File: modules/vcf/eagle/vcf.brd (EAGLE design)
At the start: 100 x 87.6 mm, 78 parts, among them IC1 TL074P, IC2 LM13700N, IC3 TL074P, Q1 2N3906, Q2 2N3906, X1 22-23-2031, X10 AUDIO INPUTS, X11 POWER, X12 FILTER OUT, X2 CV INPUTS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

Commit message: Badly finish VCF board layout (single)
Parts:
- moved R38 174.2 mm to (84.5, 12.7), turned to 90 degrees
- moved R37 148.5 mm to (65.4, 9.53), turned to 90 degrees
- moved LED5 141.4 mm to (61.6, 23.5), turned to 180 degrees
- moved R32 139.2 mm to (74.9, 33.7), turned to 180 degrees
- moved C5 134.5 mm to (77.5, 29.2), turned to 180 degrees
- moved C16 129.6 mm to (81.9, 10.2), turned to 270 degrees
- moved LED4 128.9 mm to (61.6, 38.1), turned to 180 degrees
- moved R39 126.8 mm to (93.3, 40.6), turned to 270 degrees
- moved R27 120.3 mm to (66.0, 36.2), turned to 90 degrees
- moved R20 119.7 mm to (84.5, 24.8), turned to 270 degrees
- moved R34 119.6 mm to (81.3, 62.9), turned to 90 degrees
- moved LED3 117.6 mm to (61.6, 45.1)
- moved R36 117.2 mm to (74.9, 5.71), turned to 180 degrees
- moved C11 116.5 mm to (81.9, 22.9), turned to 90 degrees
- moved R30 115.1 mm to (68.6, 30.5), turned to 90 degrees
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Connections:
- net N$1 renamed N$1V-OCT
- net N$31 renamed N$LP-OUT
- net N$40 renamed N$BP-OUT
- net N$51 renamed N$HP-OUT
- removed net N$6: X10.2, X7.2
- new net N$1: X10.1, X7.2
- net N$16: now also X10.2; no longer X10.1
- net N$37: now also IC3.13; no longer IC3.2
- net N$47: now also IC3.14; no longer IC3.1
- net N$49: now also IC3.2; no longer IC3.13
- net N$50: now also IC3.1; no longer IC3.14
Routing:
- net GND: track 31.7 -> 143.8 mm, vias 0 -> 14
- net N$37: track 0.00 -> 83.2 mm, vias 0 -> 2
- net N$47: track 0.00 -> 79.6 mm
- net N$39: track 58.8 -> 120.3 mm, vias 0 -> 2
- net N$44: track 0.00 -> 61.0 mm, vias 0 -> 4
- net N$53: track 56.0 -> 0.00 mm
- net N$50: track 0.00 -> 37.3 mm
- net N$16: track 51.8 -> 22.2 mm
- net VCC: track 146.5 -> 175.2 mm
- net VEE: track 150.8 -> 179.5 mm
- net N$48: track 0.00 -> 27.5 mm, vias 0 -> 2
- net N$BP-OUT: track 0.00 -> 27.4 mm
- net N$21: track 5.08 -> 31.3 mm
- net N$45: track 0.00 -> 25.0 mm
- net N$6: track 24.5 -> 0.00 mm
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- added copper zone on layer 16, net GND
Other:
- board size 100 x 87.6 mm -> 100 x 85.1 mm
- board text added: "VOLTAGE CONTROLLED FILTER MICHD, APR 2016"

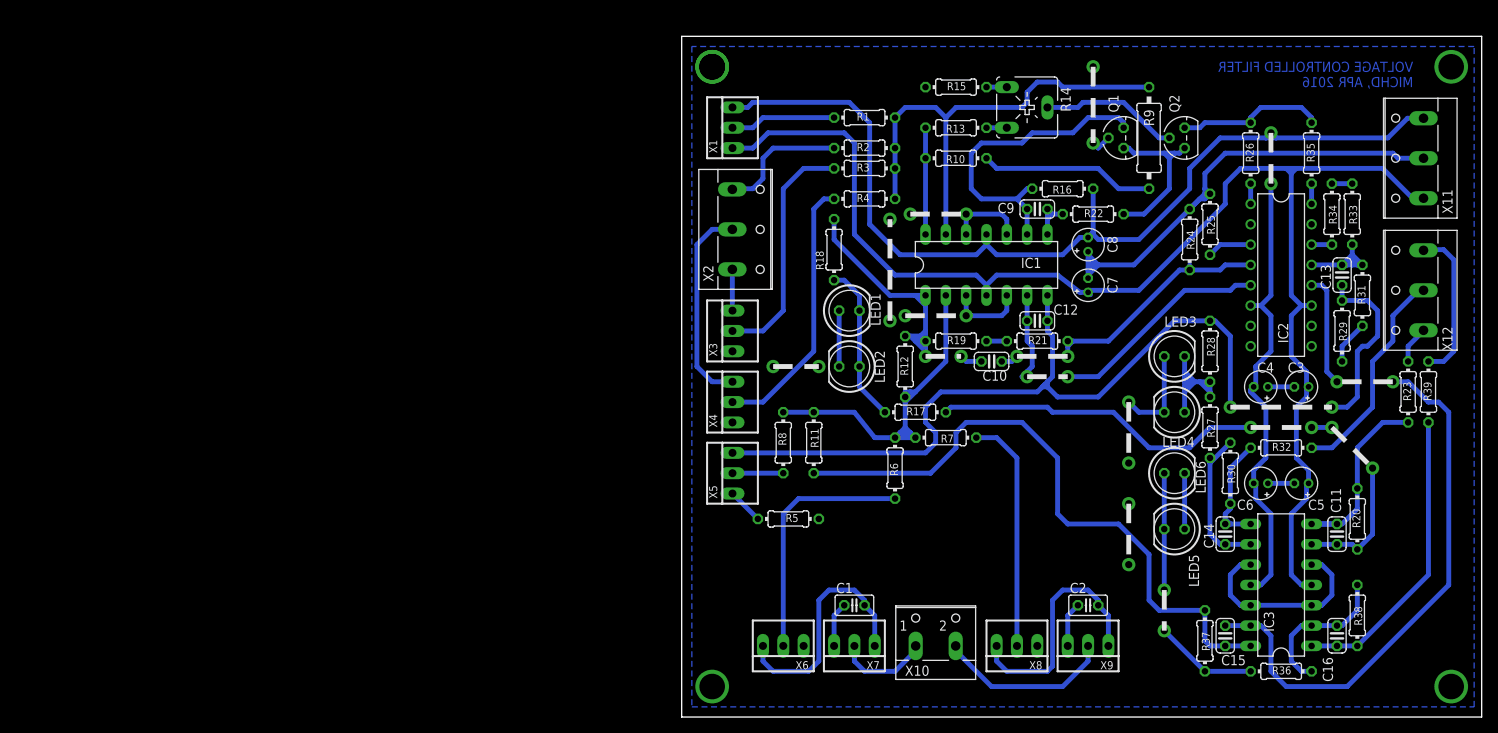
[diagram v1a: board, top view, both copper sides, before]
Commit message: Redesign filter board without limitiers; double-sided
The single-sided board with limiters didn't work. The limiters
introduced DC offsets that made various opamps just max out, creating a
static DC output. The limiting circuitry is now removed, and the new PCB
design is a double-sided one because I could not be bothered making
another terrible single-sided one.
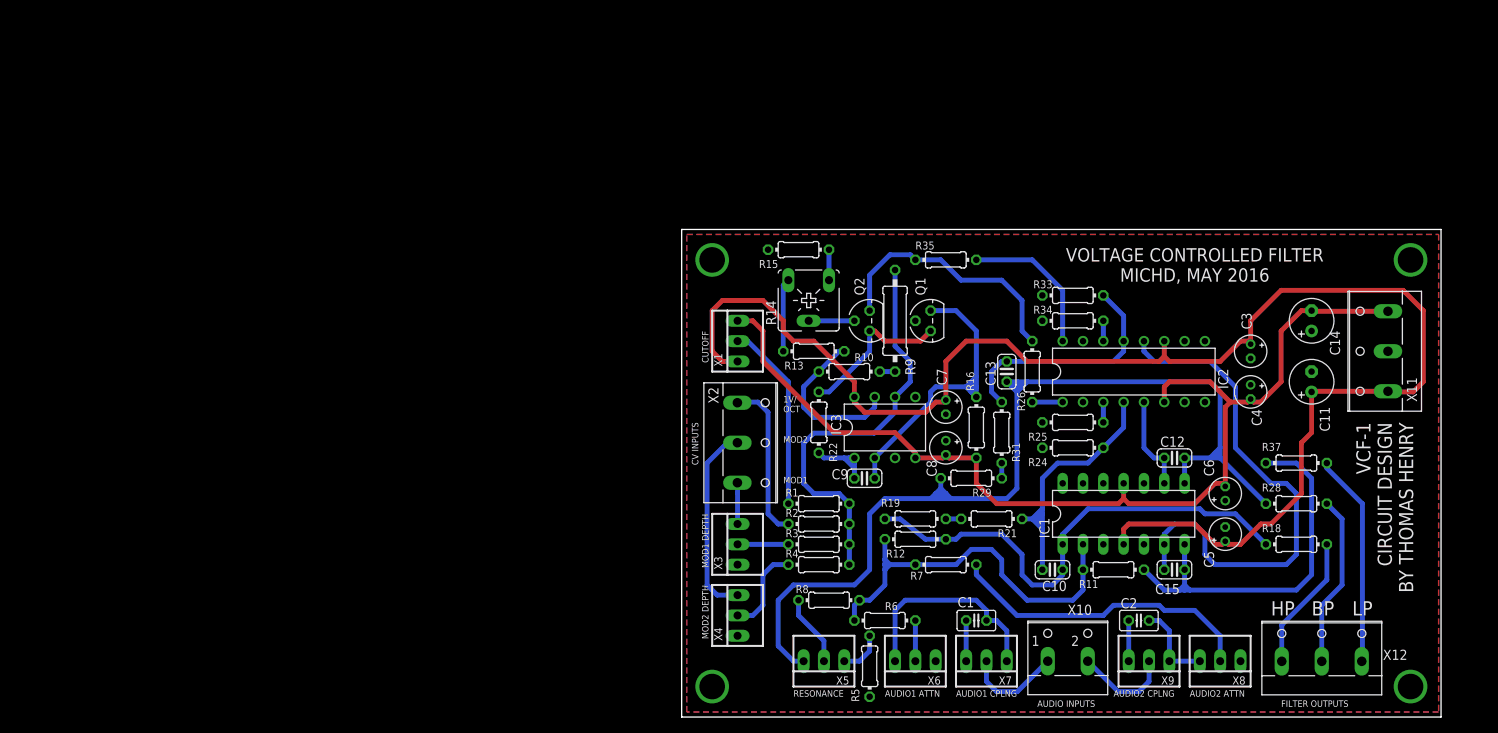
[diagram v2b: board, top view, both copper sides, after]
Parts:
- removed C16: 100p, rcl:C025-024X044
- removed LED1, LED2, LED3, LED4, LED5, LED6: RED, led:LED5MM
- removed R17, R20, R27, R30, R36, R38: 10K, rcl:0204/7
- removed R23, R32, R39: 1K, rcl:0204/7
- C11, C14: value 100p -> 470u; device rcl:C025-024X044 -> rcl:E2,5-6
- IC3: value TL074P -> TL072P; device linear:DIL14 -> linear:DIL08
- moved R18 68.5 mm to (76.8, 21.6), turned to 180 degrees
- moved IC3 53.3 mm to (25.4, 36.2), turned to 0 degrees
- moved R29 49.9 mm to (36.2, 29.8), turned to 180 degrees
- moved R1 48.6 mm to (17.1, 26.7)
- moved R31 48.2 mm to (40.0, 35.6)
- moved R35 47.6 mm to (33.0, 57.1), turned to 0 degrees
- moved R2 47.3 mm to (17.1, 24.1)
- moved R3 47.3 mm to (17.1, 21.6)
- moved X12 46.5 mm to (80.0, 8.26), turned to 0 degrees
- moved R4 46.1 mm to (17.1, 19.1)
- moved Q2 45.5 mm to (23.5, 49.5)
- moved C13 43.6 mm to (40.6, 43.2)
- moved R22 43.1 mm to (17.1, 36.8), turned to 270 degrees
- moved R11 40.7 mm to (54.0, 18.4), turned to 180 degrees
- moved C9 40.0 mm to (22.9, 29.8), turned to 180 degrees
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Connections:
- removed net N$41: LED1.K, LED2.A, R17.2, R18.1
- removed net N$42: LED3.K, LED4.A, R27.2, R28.1
- removed net N$43: C14.1, IC3.9, R27.1, R30.2
- removed net N$44: C11.1, IC3.6, R17.1, R20.2
- removed net N$45: C11.2, IC3.7, R20.1, R23.2
- removed net N$46: C14.2, IC3.8, R30.1, R32.2
- removed net N$48: LED5.K, LED6.A, R36.2, R37.1
- removed net N$49: C16.1, IC3.2, R36.1, R38.2
- removed net N$50: C16.2, IC3.1, R38.1, R39.2
- net GND: now also C11.-, C14.+, IC1.13; no longer IC3.10, IC3.12, LED1.A, LED2.K, LED3.A, LED4.K, LED5.A, LED6.K
- net N$14: now also IC3.1; no longer IC1.8
- net N$15: now also IC3.2; no longer IC1.9
- net N$29: now also IC1.9; no longer IC1.6
- net N$37: now also IC1.6; no longer IC3.13
- net N$39: now also IC1.8; no longer IC1.7
- net N$47: now also IC1.7; no longer IC3.14
- net N$9: now also IC3.7; no longer IC1.14
- net N$BP-OUT: now also R28.1; no longer R32.1
- net N$EXP-CV: now also IC3.6; no longer IC1.13
- net N$HP-OUT: now also R18.1; no longer R23.1
- net N$LP-OUT: now also R37.1; no longer R39.1
- net VCC: now also C11.+, IC3.8; no longer IC3.4
- net VEE: now also C14.-, IC3.4; no longer IC3.11
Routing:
- net GND: track 143.8 -> 0.00 mm, vias 14 -> 0
- net N$44: track 61.0 -> 0.00 mm, vias 4 -> 0
- net VEE: track 179.5 -> 129.6 mm, vias 2 -> 0
- net N$50: track 37.3 -> 0.00 mm
- net N$29: track 39.8 -> 12.0 mm, vias 2 -> 0
- net N$47: track 79.6 -> 52.1 mm
- net N$48: track 27.5 -> 0.00 mm, vias 2 -> 0
- net N$21: track 31.3 -> 5.08 mm
- net N$45: track 25.0 -> 0.00 mm
- net N$4: track 30.0 -> 6.35 mm
- net N$5: track 33.6 -> 11.2 mm
- net N$23: track 39.3 -> 61.7 mm, vias 2 -> 0
- net N$20: track 30.9 -> 10.7 mm
- net N$8: track 21.9 -> 1.91 mm
- net N$41: track 19.9 -> 0.00 mm, vias 0 -> 1
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- added copper zone on layer 1, net GND
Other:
- board size 100 x 85.1 mm -> 94.9 x 61 mm
- board text added: "1V/ OCT"
- board text added: "AUDIO INPUTS"
- board text added: "AUDIO1 ATTN"
- board text added: "AUDIO1 CPLNG"
- board text added: "AUDIO2 ATTN"
- board text added: "AUDIO2 CPLNG"
- board text added: "BP"
- board text added: "CUTOFF"
- board text added: "CV INPUTS"
- board text added: "FILTER OUTPUTS"
- board text added: "HP"
- board text added: "LP"
- board text added: "MOD1"
- board text added: "MOD1 DEPTH"
- board text added: "MOD2"
- board text added: "MOD2 DEPTH"
- board text added: "RESONANCE"
- board text added: "VCF-1 CIRCUIT DESIGN BY THOMAS HENRY"
- board text added: "VOLTAGE CONTROLLED FILTER MICHD, MAY 2016"
- board text removed: "VOLTAGE CONTROLLED FILTER MICHD, APR 2016"
